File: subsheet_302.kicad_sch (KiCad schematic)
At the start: 32 parts, among them J302 Internal FDD Power, J303 Internal FDD Port, J304 DIN-14S — External FDD Port, U301 WD1772_FLOPPY_DISK_CONTROLLER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, U305 7406_PHY

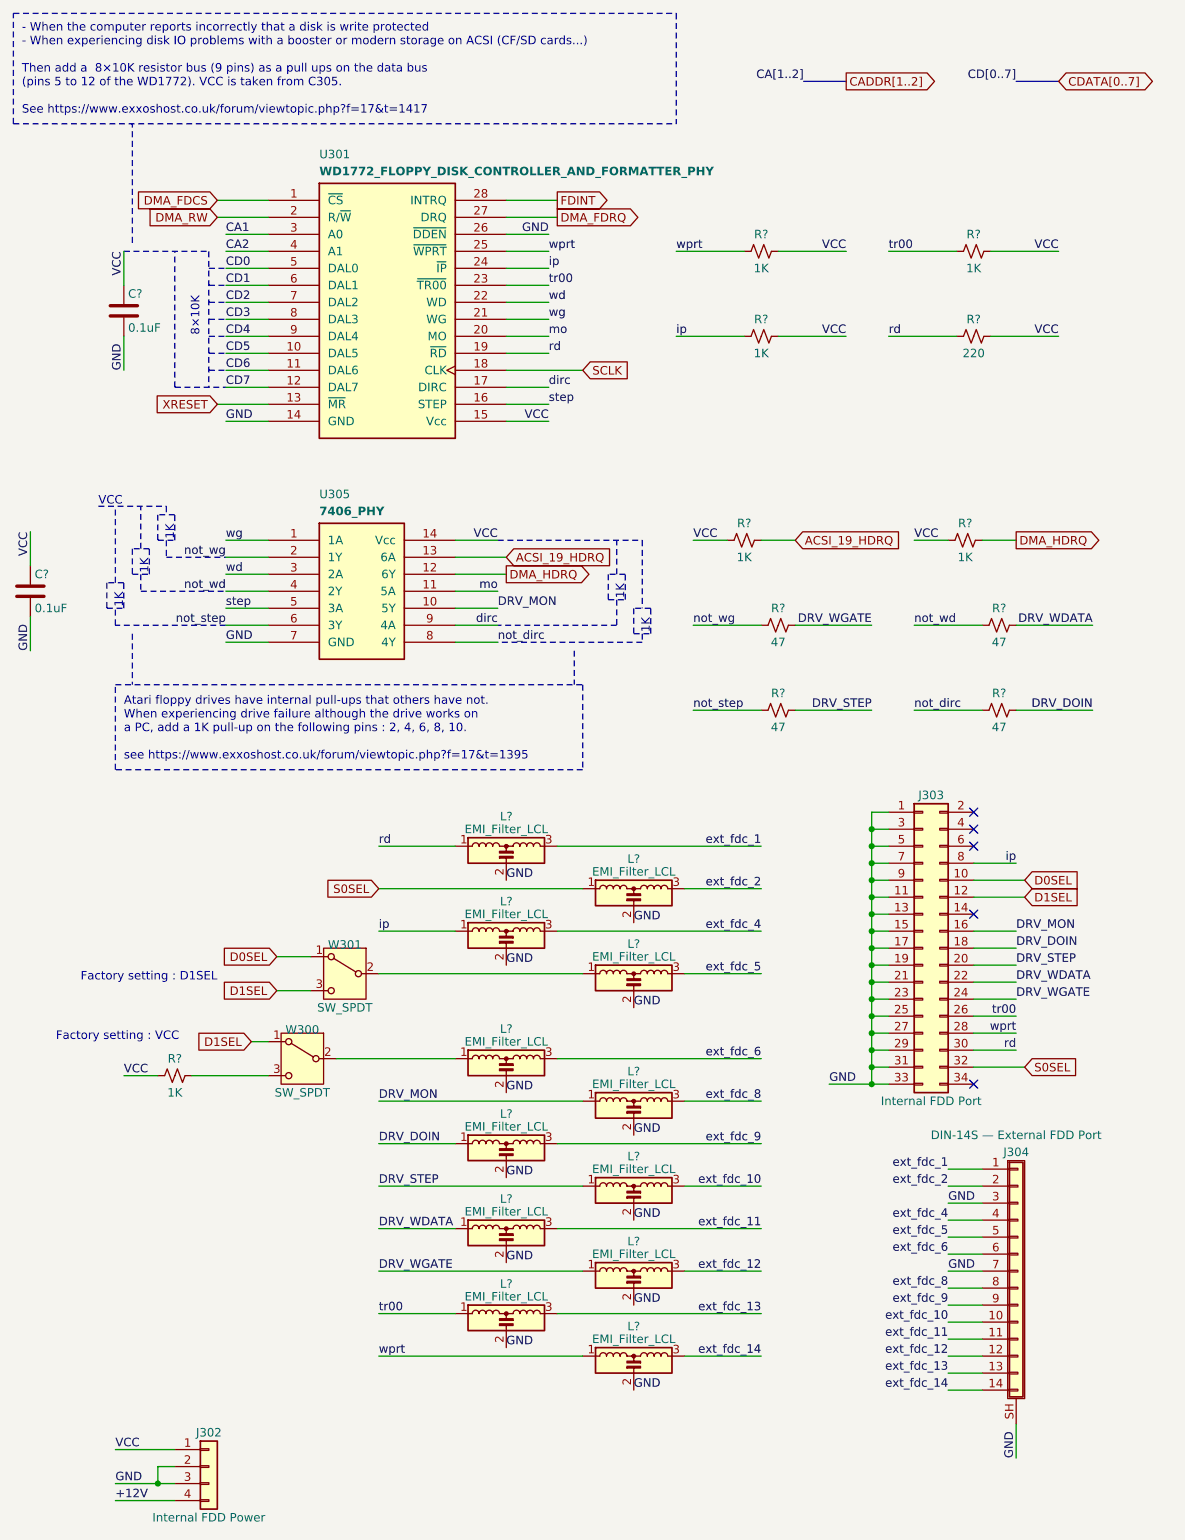
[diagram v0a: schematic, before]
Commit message: Resolves #3 : [schematic] annotate video port with signal name
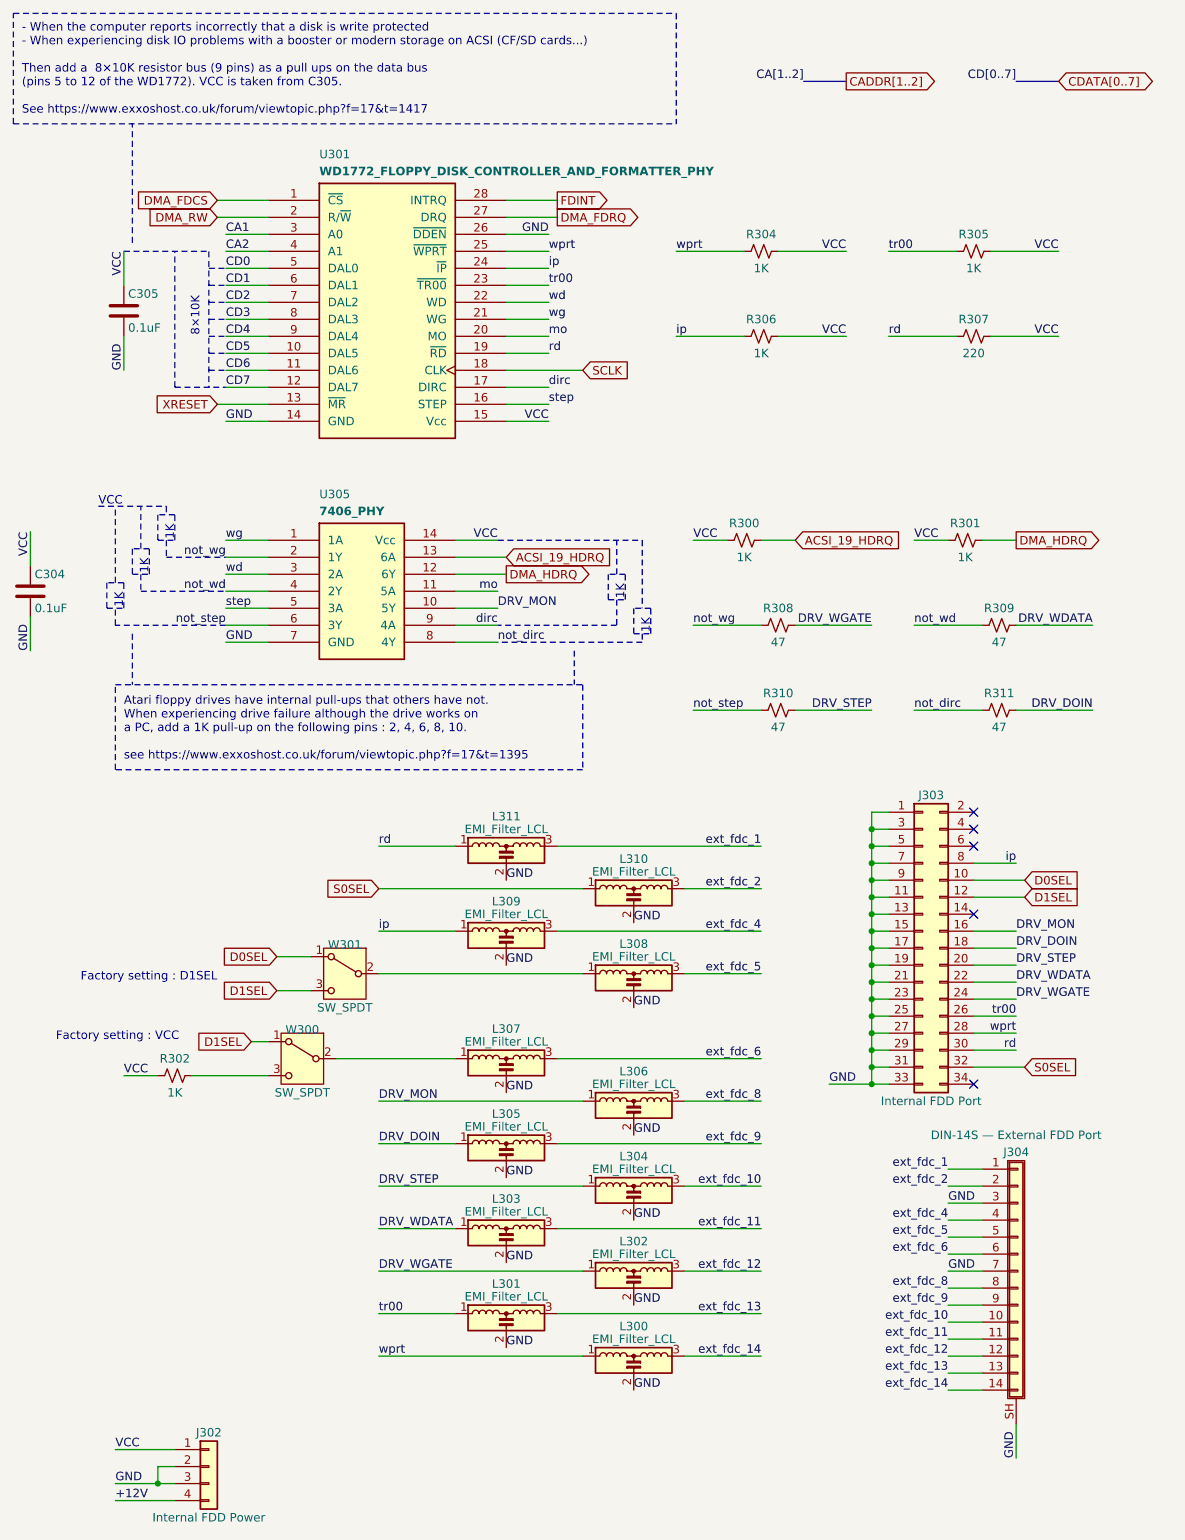
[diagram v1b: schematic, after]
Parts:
- gave numbers to parts that had none: 25
